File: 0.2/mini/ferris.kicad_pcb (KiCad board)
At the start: 2 copper layers, 208.8 x 86.8 mm, 114 parts, among them J1 TYPE-C-31-M-12, K0_0 KEYSW, K0_1 KEYSW, K0_2 KEYSW, K0_3 KEYSW, K0_4 KEYSW, K0_5 KEYSW, K0_6 KEYSW, K0_7 KEYSW, K0_8 KEYSW, K0_9 KEYSW, K1_0 KEYSW, K1_1 KEYSW, K1_2 KEYSW, K1_3 KEYSW, K1_4 KEYSW, K1_5 KEYSW, K1_6 KEYSW, K1_7 KEYSW, K1_8 KEYSW, K1_9 KEYSW, K2_0 KEYSW, K2_1 KEYSW, K2_2 KEYSW, K2_3 KEYSW, K2_4 KEYSW, K2_5 KEYSW, K2_6 KEYSW, K2_7 KEYSW, K2_8 KEYSW, K2_9 KEYSW, K3_3 KEYSW, K3_4 KEYSW, K3_5 KEYSW, K3_6 KEYSW, Q1 PDTC123JT,215, SW1 B3U-1000P, U1 STM32F072CBT6, U2 MCP23017-E/SO, U3 MCP1700T-3302E/TT, U4 SRV05-4

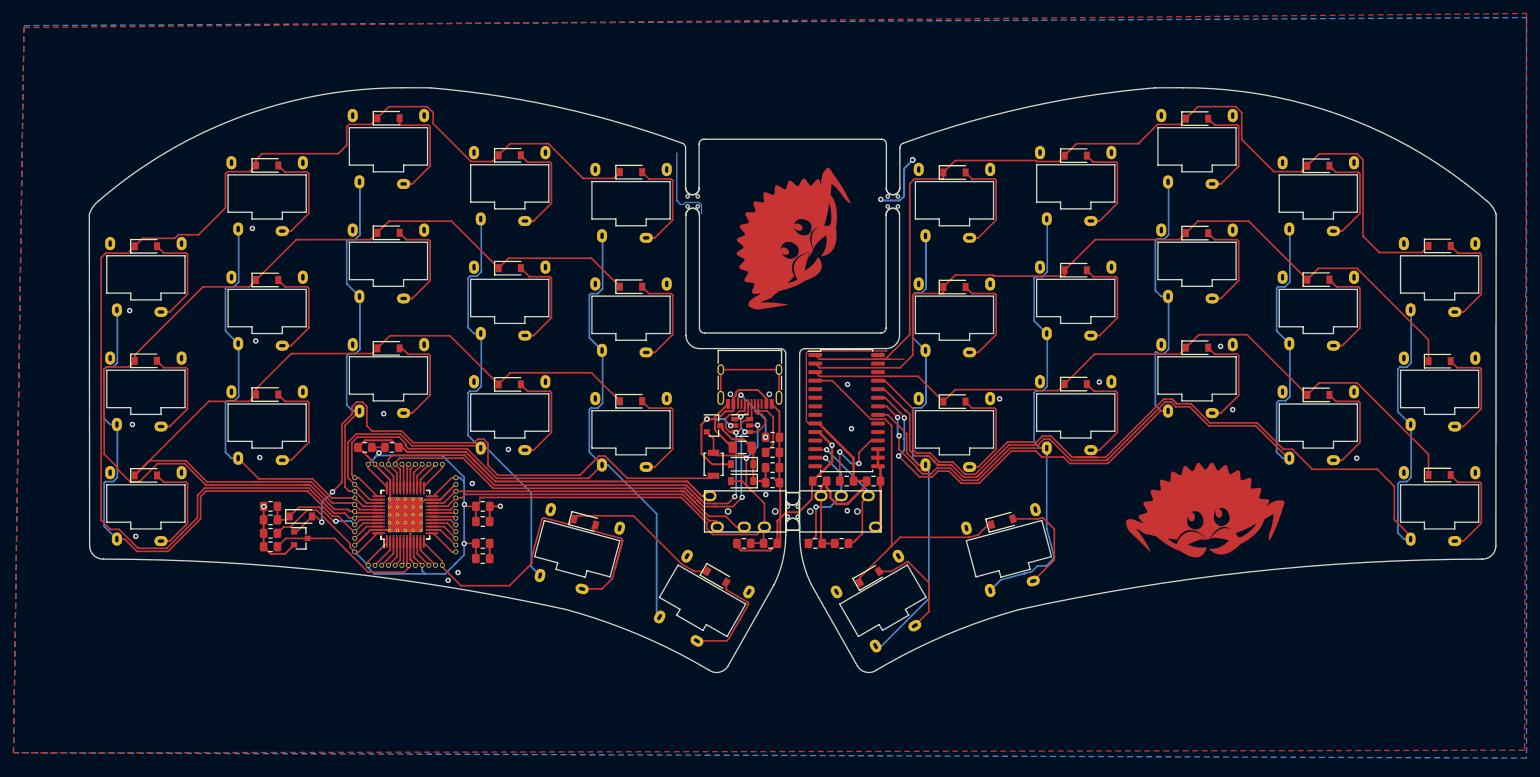
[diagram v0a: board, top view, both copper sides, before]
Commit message: Attempt to shrink the size of the mini version
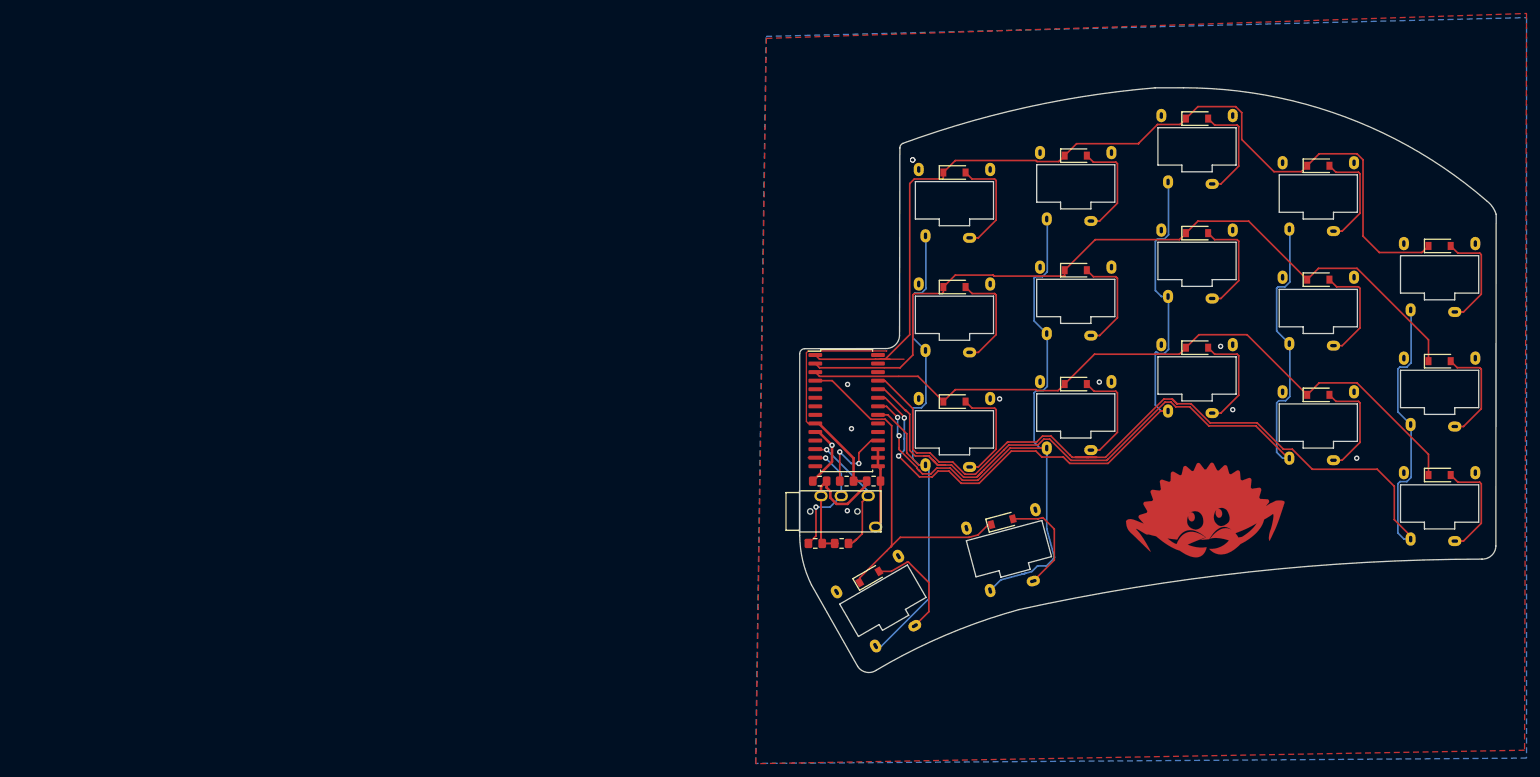
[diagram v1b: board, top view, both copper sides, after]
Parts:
- removed C1, C2, C7: 1uF, Capacitor_SMD:C_0805_2012Metric_Pad1.15x1.40mm_HandSolder
- removed C10, C5, C9: 0.1uF, Capacitor_SMD:C_0805_2012Metric_Pad1.15x1.40mm_HandSolder
- removed C11, C6: 4.7uF, Capacitor_SMD:C_0805_2012Metric_Pad1.15x1.40mm_HandSolder
- removed C3, C8: 10uF, Capacitor_SMD:C_0805_2012Metric_Pad1.15x1.40mm_HandSolder
- removed C4: 4.7nF, Capacitor_SMD:C_0805_2012Metric_Pad1.15x1.40mm_HandSolder
- removed D0_0, D0_1, D0_2, D0_3, D0_4, D1_0, D1_1, D1_2, D1_3, D1_4, D2_0, D2_1, D2_2, D2_3, D2_4, D3, D3_3, D3_4: 1N4148W, Diode_SMD:D_SOD-123
- removed D1: SMF9.0CA, Diode_SMD:D_SOD-123
- removed D2: RB060M-30TR, Diode_SMD:D_SOD-123
- removed F1: 500mA, Fuse:Fuse_1206_3216Metric
- removed the G*** at (117.1, 34.8)
- removed J1: TYPE-C-31-M-12, Connector_USB:USB_C_Receptacle_HRO_TYPE-C-31-M-12
- removed Jack0: PJ-320A, kbd:TRRS-PJ-320A
- removed K0_0, K0_1, K0_2, K0_3, K0_4, K1_0, K1_1, K1_2, K1_3, K1_4, K2_0, K2_1, K2_2, K2_3, K2_4, K3_3, K3_4: KEYSW, switches:Choc_Mini_PG1232_Choc_Spacing
- removed Q1: PDTC123JT,215, Package_TO_SOT_SMD:SOT-23
- removed R1, R2: 5.1kΩ, Resistor_SMD:R_0805_2012Metric_Pad1.15x1.40mm_HandSolder
- removed R3, R4, R5: 100kΩ, Resistor_SMD:R_0805_2012Metric_Pad1.15x1.40mm_HandSolder
- removed the REF** at (110.4, 65.6)
- removed the REF** at (59.3, 73.5)
- removed the REF** at (25.9, 31.1)
- removed SW1: B3U-1000P, Button_Switch_SMD:SW_SPST_B3U-1000P
- removed U1: STM32F072CBT6, breakout_pins:Dual_MCU_QFP_QFN_48_with_breakout_pins
- removed U3: MCP1700T-3302E/TT, Package_TO_SOT_SMD:SOT-23
- removed U4: SRV05-4, Package_TO_SOT_SMD:SOT-23-6
- removed mouse-bite-2mm-slot (x3): VAL**, panelization:mouse-bite-2mm-slot-with-space-for-track
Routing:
- net GND: track 218.9 -> 22.2 mm, vias 28 -> 11
- net /row0,0: track 188.3 -> 0.00 mm
- net +3V3: track 182.9 -> 0.00 mm, vias 5 -> 0
- net /row0,1: track 151.9 -> 0.00 mm
- net /row0,2: track 129.0 -> 0.00 mm
- net /col4: track 115.9 -> 0.00 mm
- net /col3: track 94.1 -> 0.00 mm
- net Net-(D3-Pad2): track 89.6 -> 0.00 mm, vias 2 -> 0
- net /col0: track 87.3 -> 0.00 mm
- net /D-: track 84.1 -> 0.00 mm, vias 3 -> 0
- net /D+: track 83.4 -> 0.00 mm, vias 2 -> 0
- net /col1: track 62.4 -> 0.00 mm
- net /col2: track 56.7 -> 0.00 mm
- net /row0,3: track 55.5 -> 0.00 mm
- net i2c_sda: track 54.6 -> 0.00 mm
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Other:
- board size 208.8 x 86.8 mm -> 103.4 x 86.8 mm
- net class Default removed
- net class Power removed
- board text removed: "Ferris Mini - v0.2.1 by @pierrec83 As low profile as it gets! * Split, 34 Keys * Kailh Choc Mini: pg1232 * Choc spacing: 17x18mm * Microcontroller: STM32FO72 * IO Expander: MCP23017 * USB C * All mcu pins broken out * Dimensions: 104x87mm per side Fully open source design: github.com/pierrechevalier83/ferris"
- board text removed: "by @pierrec83 and @bomtarnes"
